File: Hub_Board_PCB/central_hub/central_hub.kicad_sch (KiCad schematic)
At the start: 69 parts, among them J1 CX90B-16P, J2 Barrel_Jack_Switch, J3 TSM-105-01-S-DV-M-TR, J4 Screw_Terminal_01x08, J5 PH2-06-UA, J6 Screw_Terminal_01x04, J7 Screw_Terminal_01x14, SW1 RotaryEncoder_Switch, SW2 SW_Push, U1 R7FA4M1AB3CFM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

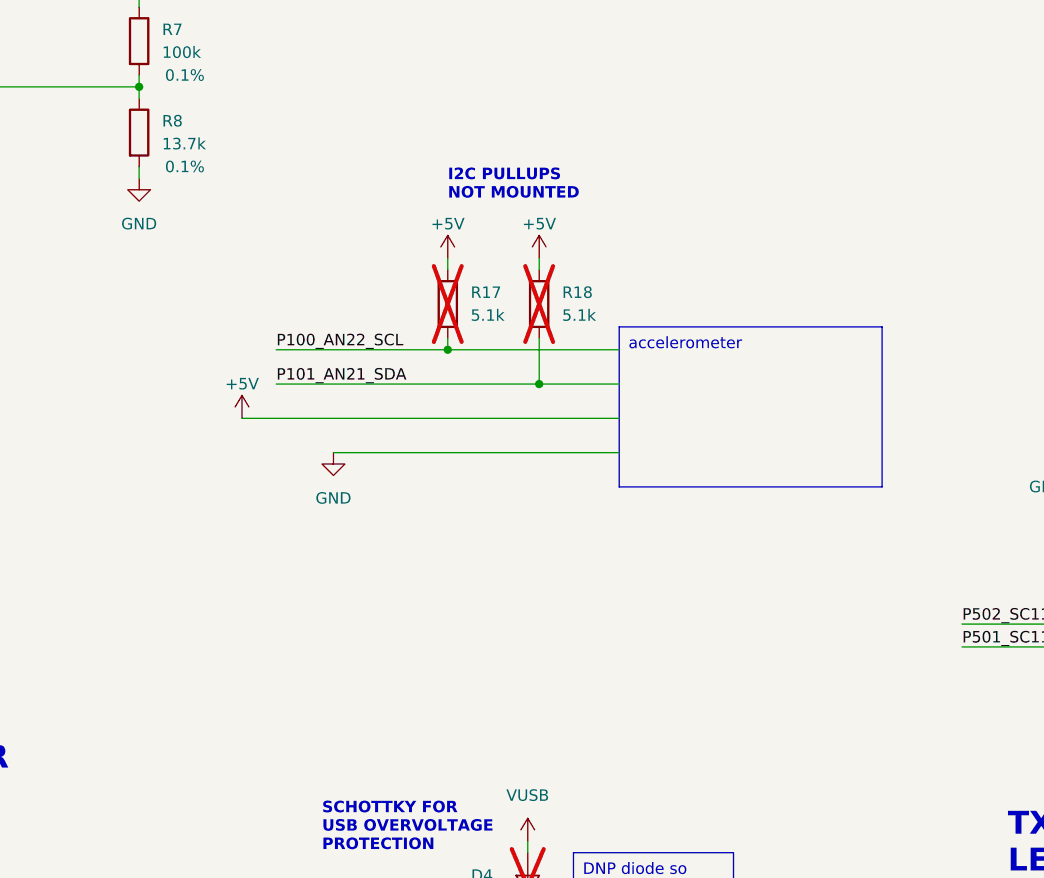
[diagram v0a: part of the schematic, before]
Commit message: added accelerometer
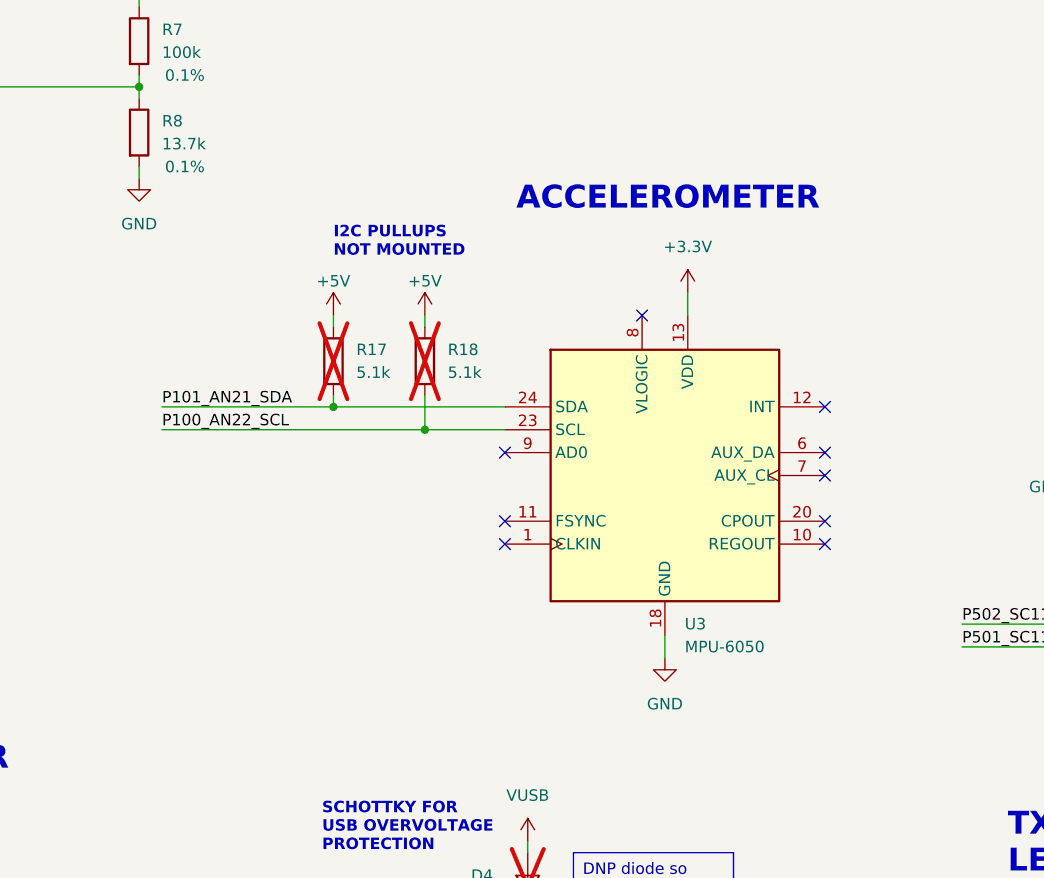
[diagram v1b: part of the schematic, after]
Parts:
- added U3: MPU-6050, Sensor_Motion:InvenSense_QFN-24_4x4mm_P0.5mm, symbol Sensor_Motion:MPU-6050
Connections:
- net +3.3V: now also U3.13 (VDD)
- net GND: now also U3.18 (GND)
- net P100_AN22_SCL: now also R18.2, U3.23 (SCL); no longer R17.2
- net P101_AN21_SDA: now also R17.2, U3.24 (SDA); no longer R18.2
- no-connect marks 0 -> 9
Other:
- note added: "ACCELEROMETER"
- moved on the sheet: R17, R18

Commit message: Nov 1st Meeting. Addressed comments, updated hub board sheets
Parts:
- removed C1, C10, C2, C3, C4, C5, C7, C8, C9: 15pF, symbol Device:C
- removed C11: 4.7nF, symbol Device:C
- removed C12, C13, C16, C17: 22uF, symbol Device:C
- removed C14: 100nF, symbol Device:C
- removed C15: 10uF, symbol Device:C
- removed C6: 4.7uF, symbol Device:C
- removed D1: PRTR5V0U2X,215, Package_TO_SOT_SMD:SOT-143, symbol Power_Protection:PRTR5V0U2X
- removed D2, D4: PMEG6020AELRX, Diode_SMD:Nexperia_CFP3_SOD-123W, symbol Diode:PMEG6020AELR
- removed D3, D5, D6, D7: LED, symbol Device:LED
- removed J1: CX90B-16P, CON18_1X12_P0_HIR, symbol CX90B-16P:CX90B-16P
- removed J2: Barrel_Jack_Switch, symbol Connector:Barrel_Jack_Switch
- removed J3: TSM-105-01-S-DV-M-TR, CONN_TSM-105-01-S-DV-M-TR_SAI, symbol TSM-105-01-S-DV-M-TR:TSM-105-01-S-DV-M-TR
- removed J4: Screw_Terminal_01x08, symbol Connector:Screw_Terminal_01x08
- removed J5: PH2-06-UA, CONN_PH2-06-UA_ADM, symbol PH2-06-UA:PH2-06-UA
- removed J6: Screw_Terminal_01x04, symbol Connector:Screw_Terminal_01x04
- removed J7: Screw_Terminal_01x14, symbol Connector:Screw_Terminal_01x14
- removed L1, L2: BLM18PG471SN1D, IND_BLM18_0603_MUR, symbol BLM18PG471SN1D:BLM18PG471SN1D
- removed L3: 4.7uH, symbol Device:L
- removed R1, R10, R11, R16, R17, R18, R2, R3, R4, R5, R6: 5.1k, symbol Device:R
- removed R12, R13, R14, R15: 330, symbol Device:R
- removed R7: 100k, symbol Device:R
- removed R8: 13.7k, symbol Device:R
- removed R9: 1M, symbol Device:R
- removed SW1: RotaryEncoder_Switch, symbol Device:RotaryEncoder_Switch
- removed SW2: SW_Push, symbol Switch:SW_Push
- removed TP1, TP10, TP11, TP2, TP3, TP4, TP5, TP6, TP7, TP8, TP9, love: TestPoint, symbol Connector:TestPoint
- removed U1: R7FA4M1AB3CFM, PLQP0064KB-C_REN, symbol R7FA4M1AB3CFM:R7FA4M1AB3CFM
- removed U2: AP63205WU-7, SOIC_05WU-7_DIO, symbol AP63205WU-7:AP63205WU-7
- removed U3: MPU-6050, Sensor_Motion:InvenSense_QFN-24_4x4mm_P0.5mm, symbol Sensor_Motion:MPU-6050
- removed Y1: 16MHz?, symbol Device:Crystal
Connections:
- no-connect marks 9 -> 0
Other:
- added sheet Accelerometer (Accelerometer_Sheet.kicad_sch)
- added sheet CAN (CAN_Sheet.kicad_sch)
- added sheet MCU (MCU_Sheet.kicad_sch)
- added sheet Power (Power_Sheet.kicad_sch)
- note removed: "ACCELEROMETER"
- note removed: "ANALOG HEADER"
- note removed: "BUCK CONVERTER"
- note removed: "CC RESISTORS"
- note removed: "CS"
- note removed: "DAC"
- note removed: "DC JACK"
- note removed: "DIGITAL HEADER"
- note removed: "ESD PROTECTION"
- note removed: "GPS HEADER"
- note removed: "GREEN"
- note removed: "I2C PULLUPS NOT MOUNTED"
- note removed: "ICSP HEADER"
- note removed: "INPUT ONLY"
- note removed: "MICROCONTROLLER"
- note removed: "MISO"
- note removed: "MOSI"
- note removed: "OPAMP OUT"
- note removed: "OPAMP+"
- note removed: "OPAMP-"
- note removed: "POWER LED"
- note removed: "RESET PUSHBUTTON"
- note removed: "RX"
- note removed: "RX LED"
- note removed: "RX on GPS"
- note removed: "SCHOTTKY FOR REVERSE POLARITY PROTECTION"
- note removed: "SCHOTTKY FOR USB OVERVOLTAGE PROTECTION"
- note removed: "SCK"
- note removed: "SCK LED"
- note removed: "SWD CONNECTOR"
- note removed: "TESTPOINTS"
- note removed: "TX"
- note removed: "TX LED"
- note removed: "TX on GPS"
- note removed: "USB CONNECTOR"
- note removed: "USB LDO OUTPUT"
- note removed: "VCL is the output of the internal LDO"
- note removed: "YELLOW"
- note removed: "diff pair"

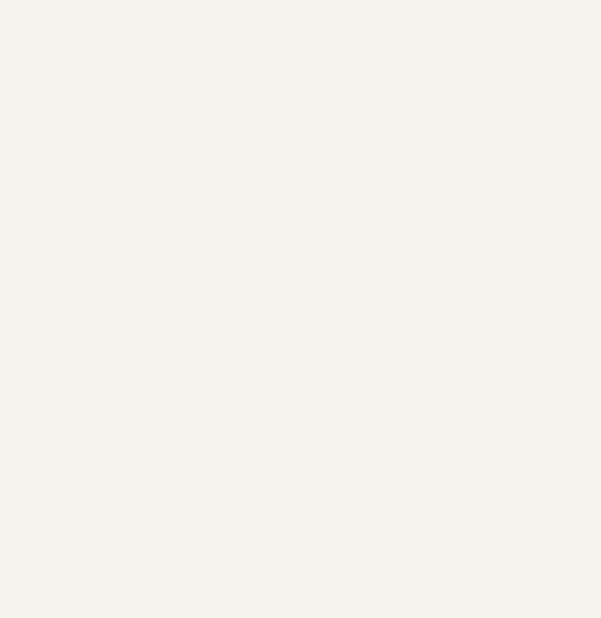
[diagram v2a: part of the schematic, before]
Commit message: - added global net-labels and reorganized pages - 4.0" TFT SPI 480*320 V2.1 display may already have a level-shifter (actually has HR2046, touch screen controller) so may not need to include voltage dividers and NMOSes
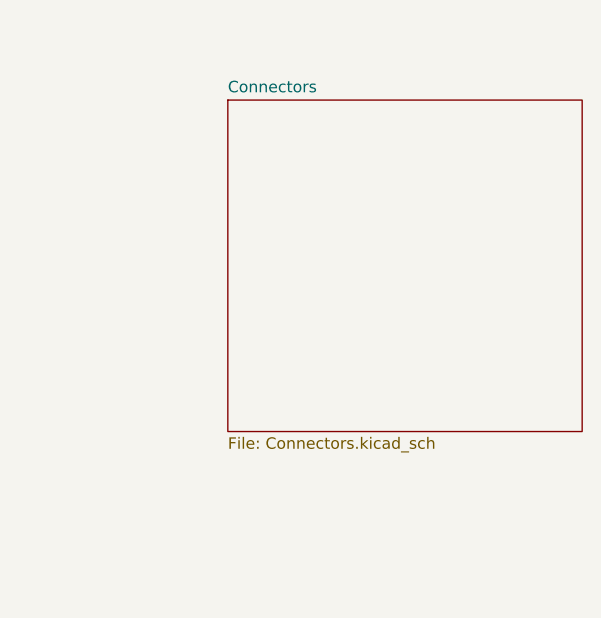
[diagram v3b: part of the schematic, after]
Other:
- added sheet Connectors (Connectors.kicad_sch)
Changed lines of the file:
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@@
+    )
+  )
+  (sheet (at 308.61 30.48) (size 39.37 36.83) (fields_autoplaced)
+    (stroke (width 0.1524) (type solid))
+    (fill (color 0 0 0 0.0000))
+    (property "Sheetname" "Connectors" (at 308.61 29.7684 0)
+      (effects (font (size 1.27 1.27)) (justify left bottom))
+    )
+    (property "Sheetfile" "Connectors.kicad_sch" (at 308.61 67.8946 0)
+      (effects (font (size 1.27 1.27)) (justify left top))
+    )
+    (instances
+      (project "central_hub"
+        (path "/0d9ec66e-0fbf-4d12-9b83-adf78971a00b" (page "6"))
+      )
     )
   )

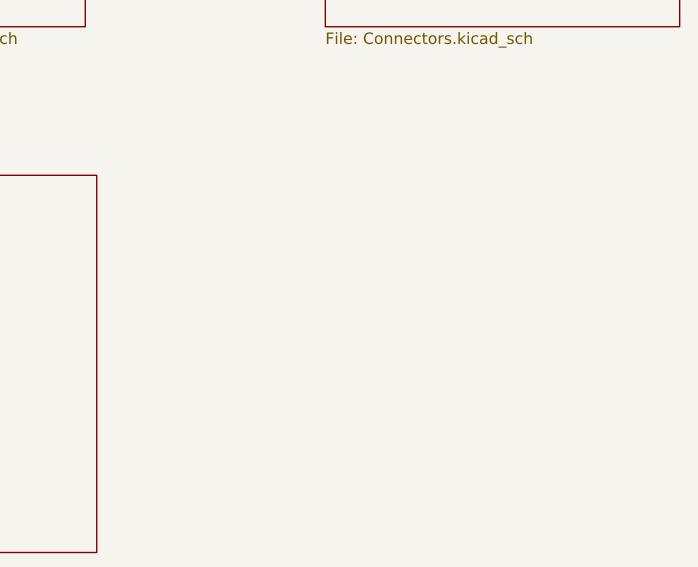
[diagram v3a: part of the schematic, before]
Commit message: Added new connectors as per brandons new shifters
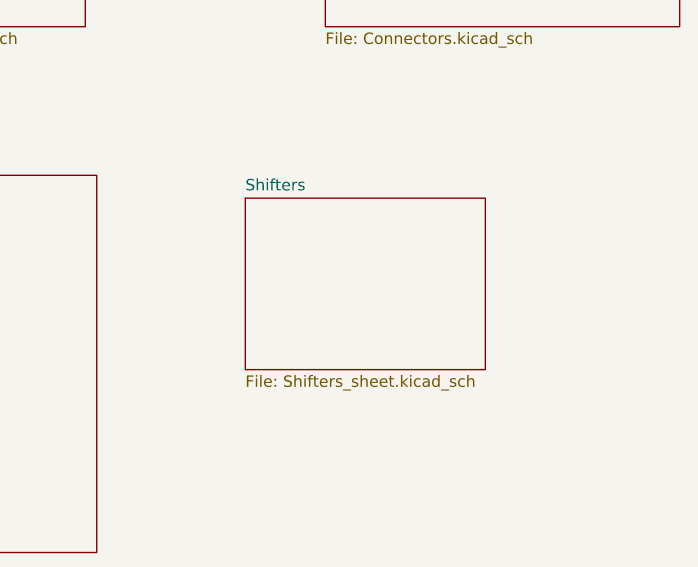
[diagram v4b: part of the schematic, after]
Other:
- added sheet Shifters (Shifters_sheet.kicad_sch)
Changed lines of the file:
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@@
 (kicad_sch (version 20230121) (generator eeschema)
   (paper "A3")
+  (sheet (at 299.72 86.36) (size 26.67 19.05) (fields_autoplaced)
+    (stroke (width 0.1524) (type solid))
+    (fill (color 0 0 0 0.0000))
+    (property "Sheetname" "Shifters" (at 299.72 85.6484 0)
+      (effects (font (size 1.27 1.27)) (justify left bottom))
+    )
+    (property "Sheetfile" "Shifters_sheet.kicad_sch" (at 299.72 105.9946 0)
+      (effects (font (size 1.27 1.27)) (justify left top))
+    )
+    (instances
+      (project "central_hub"
+        (path "/0d9ec66e-0fbf-4d12-9b83-adf78971a00b" (page "7"))
+      )
+    )
+  )
   (sheet (at 242.57 30.48) (size 39.37 36.83) (fields_autoplaced)
     (stroke (width 0.1524) (type solid))
